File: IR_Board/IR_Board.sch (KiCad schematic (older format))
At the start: 16 parts, among them J1 Conn_02x08_Row_Letter_First, U1 TSSP58038, U10 TSSP58038, U11 TSSP58038, U12 TSSP58038, U13 TSSP58038, U14 TSSP58038, U2 TSSP58038, U3 TSSP58038, U4 TSSP58038, U5 TSSP58038, U6 TSSP58038, U7 TSSP58038, U8 TSSP58038, U9 TSSP58038

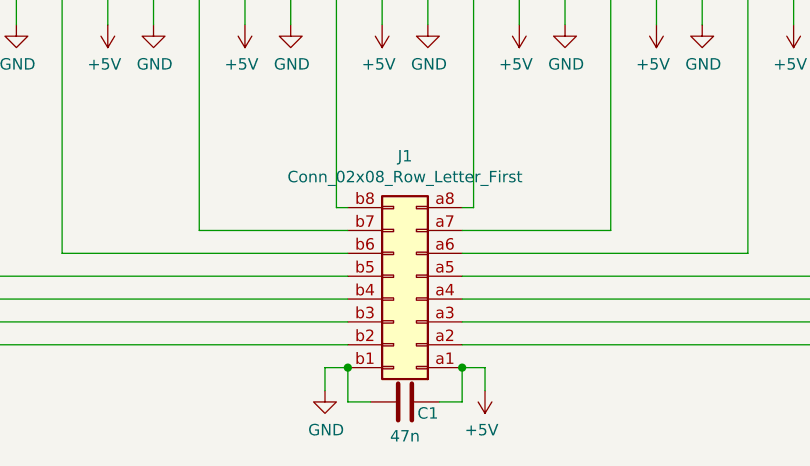
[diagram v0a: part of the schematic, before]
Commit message: motor drivers added
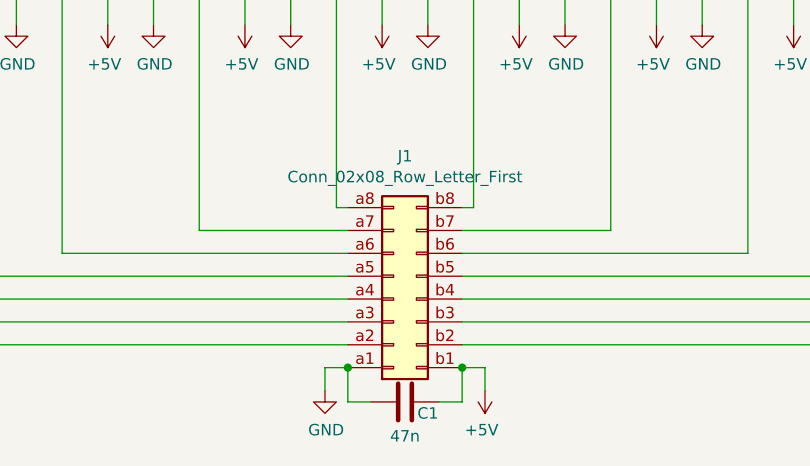
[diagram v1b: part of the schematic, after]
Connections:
- net +5V: now also J1.b1 (Pin_b1); no longer J1.a1 (Pin_a1)
- net GND: now also J1.a1 (Pin_a1); no longer J1.b1 (Pin_b1)
- net at U1.1 (OUT): now also J1.a2 (Pin_a2); no longer J1.b2 (Pin_b2)
- net at U2.1 (OUT): now also J1.a3 (Pin_a3); no longer J1.b3 (Pin_b3)
- net at U3.1 (OUT): now also J1.a4 (Pin_a4); no longer J1.b4 (Pin_b4)
- net at U4.1 (OUT): now also J1.a5 (Pin_a5); no longer J1.b5 (Pin_b5)
- net at U5.1 (OUT): now also J1.a6 (Pin_a6); no longer J1.b6 (Pin_b6)
- net at U6.1 (OUT): now also J1.a7 (Pin_a7); no longer J1.b7 (Pin_b7)
- net at U7.1 (OUT): now also J1.a8 (Pin_a8); no longer J1.b8 (Pin_b8)
- net at U8.1 (OUT): now also J1.b8 (Pin_b8); no longer J1.a8 (Pin_a8)
- net at U9.1 (OUT): now also J1.b7 (Pin_b7); no longer J1.a7 (Pin_a7)
- net at U10.1 (OUT): now also J1.b6 (Pin_b6); no longer J1.a6 (Pin_a6)
- net at U11.1 (OUT): now also J1.b5 (Pin_b5); no longer J1.a5 (Pin_a5)
- net at U12.1 (OUT): now also J1.b4 (Pin_b4); no longer J1.a4 (Pin_a4)
- net at U13.1 (OUT): now also J1.b3 (Pin_b3); no longer J1.a3 (Pin_a3)
- net at U14.1 (OUT): now also J1.b2 (Pin_b2); no longer J1.a2 (Pin_a2)
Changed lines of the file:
@@
 Wire Wire Line
 	9950 1900 9950 1750
-$Comp
-L Connector_Generic:Conn_02x08_Row_Letter_First J1
-U 1 1 61A6AA53
-P 5900 3100
-F 0 "J1" H 5950 2475 50  0000 C CNN
-F 1 "Conn_02x08_Row_Letter_First" H 5950 2566 50  0000 C CNN
-F 2 "Connector_JST:JST_PHD_B16B-PHDSS_2x08_P2.00mm_Vertical" H 5900 3100 50  0001 C CNN
-F 3 "~" H 5900 3100 50  0001 C CNN
-	1    5900 3100
-	-1   0    0    1
-$EndComp
 Wire Wire Line
 	1950 1750 1950 3300
@@
 	6150 2700 6150 1750
 Wire Wire Line
-	6100 2800 6750 2800
-Wire Wire Line
 	6750 2800 6750 1750
 Wire Wire Line
 	7350 1750 7350 2900
 Wire Wire Line
-	7350 2900 6100 2900
-Wire Wire Line
 	7950 1750 7950 3000
-Wire Wire Line
-	7950 3000 6100 3000
 Wire Wire Line
 	8550 1750 8550 3100
 Wire Wire Line
-	8550 3100 6100 3100
-Wire Wire Line
 	9150 1750 9150 3200
 Wire Wire Line
-	9150 3200 6100 3200
-Wire Wire Line
 	9750 1750 9750 3300
-Wire Wire Line
-	9750 3300 6100 3300
 $Comp
 L power:+5V #PWR0129
@@
 Wire Wire Line
 	5600 3550 5600 3400
-Connection ~ 5600 3400
 Wire Wire Line
 	6000 3550 6100 3550
@@
 	6100 3550 6100 3400
 Connection ~ 6100 3400
+Connection ~ 5600 3400
+Wire Wire Line
+	6100 2800 6750 2800
+Wire Wire Line
+	7350 2900 6100 2900
+Wire Wire Line
+	7950 3000 6100 3000
+Wire Wire Line
+	8550 3100 6100 3100
+Wire Wire Line
+	9150 3200 6100 3200
+Wire Wire Line
+	9750 3300 6100 3300
+$Comp
+L Connector_Generic:Conn_02x08_Row_Letter_First J1
+U 1 1 61A6AA53
+P 5800 3100
+F 0 "J1" H 5850 2475 50  0000 C CNN
+F 1 "Conn_02x08_Row_Letter_First" H 5850 2566 50  0000 C CNN
+F 2 "Connector_JST:JST_PHD_B16B-PHDSS_2x08_P2.00mm_Vertical" H 5800 3100 50  0001 C CNN
+F 3 "~" H 5800 3100 50  0001 C CNN
+	1    5800 3100
+	1    0    0    1
+$EndComp
 $EndSCHEMATC

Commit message: Started Light PCB
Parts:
- added C10, C11, C12, C13, C14, C15, C2, C3, C4, C5, C6, C7, C8, C9: 220n, Capacitor_SMD:C_0603_1608Metric_Pad1.08x0.95mm_HandSolder, symbol Device:C_Small
- added D1: B, LED_SMD:LED_0805_2012Metric_Pad1.15x1.40mm_HandSolder, symbol Device:LED
- added D2: A, LED_SMD:LED_0805_2012Metric_Pad1.15x1.40mm_HandSolder, symbol Device:LED_ALT
- added Q1, Q10, Q11, Q12, Q13, Q14, Q2, Q3, Q4, Q5, Q6, Q7, Q8, Q9: FDG1024NZ, Package_TO_SOT_SMD:SOT-363_SC-70-6, symbol Transistor_FET:FDG1024NZ
- added R1, R10, R11, R12, R13, R14, R15, R16, R17, R2, R3, R4, R5, R6, R7, R8, R9: 10k, Resistor_SMD:R_0603_1608Metric_Pad0.98x0.95mm_HandSolder, symbol Device:R_Small
- added SW1: SW_SPDT, Connector_PinHeader_2.54mm:PinHeader_1x03_P2.54mm_Vertical, symbol Switch:SW_SPDT
- C1: footprint Capacitor_SMD:C_0603_1608Metric_Pad1.05x0.95mm_HandSolder -> Capacitor_SMD:C_0603_1608Metric_Pad1.08x0.95mm_HandSolder
- J1: value Conn_02x08_Row_Letter_First -> CONN_OUT
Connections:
- net +5V: now also R9.2, SW1.2 (B)
- net GND: now also C10.1, C11.1, C12.1, C13.1, C14.1, C15.1, C2.1, C3.1, C4.1, C5.1, C6.1, C7.1, C8.1, C9.1, D1.1 (K), D2.1 (K), R9.1
- net at U1.1 (OUT): now also Q1.6 (D), Q2.6 (D); no longer J1.a2 (Pin_a2)
- net at U2.1 (OUT): now also Q3.6 (D), Q4.6 (D); no longer J1.a3 (Pin_a3)
- net at U3.1 (OUT): now also Q5.6 (D), Q6.6 (D); no longer J1.a4 (Pin_a4)
- net at U4.1 (OUT): now also Q7.6 (D), Q8.6 (D); no longer J1.a5 (Pin_a5)
- net at U5.1 (OUT): now also Q10.3 (D), Q9.3 (D); no longer J1.a6 (Pin_a6)
- net at U6.1 (OUT): now also Q11.6 (D), Q12.6 (D); no longer J1.a7 (Pin_a7)
- net at U7.1 (OUT): now also Q13.6 (D), Q14.6 (D); no longer J1.a8 (Pin_a8)
- net at U8.1 (OUT): now also Q1.3 (D), Q2.3 (D); no longer J1.b8 (Pin_b8)
- net at U9.1 (OUT): now also Q3.3 (D), Q4.3 (D); no longer J1.b7 (Pin_b7)
- net at U10.1 (OUT): now also Q5.3 (D), Q6.3 (D); no longer J1.b6 (Pin_b6)
- net at U11.1 (OUT): now also Q7.3 (D), Q8.3 (D); no longer J1.b5 (Pin_b5)
- net at U12.1 (OUT): now also Q10.6 (D), Q9.6 (D); no longer J1.b4 (Pin_b4)
- net at U13.1 (OUT): now also Q11.3 (D), Q12.3 (D); no longer J1.b3 (Pin_b3)
- net at U14.1 (OUT): now also Q13.3 (D), Q14.3 (D); no longer J1.b2 (Pin_b2)
- new net: C2.2, J1.a2 (Pin_a2), Q1.1 (S), R2.2
- new net: C4.2, J1.a3 (Pin_a3), Q3.1 (S), R4.2
- new net: C6.2, J1.a4 (Pin_a4), Q5.1 (S), R6.2
- new net: C8.2, J1.a5 (Pin_a5), Q7.1 (S), R8.2
- new net: J1.a6 (Pin_a6), Q9.4 (S)
- new net: J1.a7 (Pin_a7), Q11.1 (S), R15.2
- new net: J1.a8 (Pin_a8), Q13.1 (S), R17.2
- new net: C3.2, J1.b2 (Pin_b2), Q2.4 (S), R1.2
- new net: C5.2, J1.b3 (Pin_b3), Q4.4 (S), R3.2
- new net: C7.2, J1.b4 (Pin_b4), Q6.4 (S), R5.2
- new net: C9.2, J1.b5 (Pin_b5), Q8.4 (S), R7.2
- new net: C10.2, J1.b6 (Pin_b6), Q10.1 (S), R10.2
- new net: C13.2, J1.b7 (Pin_b7), Q12.4 (S), R14.2
- new net: C15.2, J1.b8 (Pin_b8), Q14.4 (S), R16.2
- new net: Q2.1 (S), R2.1
- new net: Q4.1 (S), R4.1
- new net: Q6.1 (S), R6.1
- new net: Q8.1 (S), R8.1
- new net: Q10.4 (S), R11.1
- new net: Q12.1 (S), R15.1
- new net: Q14.1 (S), R17.1
- new net: Q13.4 (S), R16.1
- new net: Q11.4 (S), R14.1
- new net: Q9.1 (S), R10.1
- new net: Q7.4 (S), R7.1
- new net: Q5.4 (S), R5.1
- new net: Q3.4 (S), R3.1
- new net: Q1.4 (S), R1.1
- new net: C11.2, R11.2
- new net: D2.2 (A), R13.1
- new net: D1.2 (A), R12.1
- new net A: Q1.2 (G), Q1.5 (G), Q10.2 (G), Q11.2 (G), Q12.5 (G), Q13.2 (G), Q14.5 (G), Q2.5 (G), Q3.2 (G), Q4.5 (G), Q5.2 (G), Q6.5 (G), Q7.2 (G), Q8.5 (G), Q9.5 (G), R13.2, SW1.3 (C)
- new net B: Q10.5 (G), Q11.5 (G), Q12.2 (G), Q13.5 (G), Q14.2 (G), Q2.2 (G), Q3.5 (G), Q4.2 (G), Q5.5 (G), Q6.2 (G), Q7.5 (G), Q8.2 (G), Q9.2 (G), R12.2, SW1.1 (A)
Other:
- moved on the sheet: C1, J1, U1, U10, U11, U12, U13, U14, U2, U3, U4, U5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

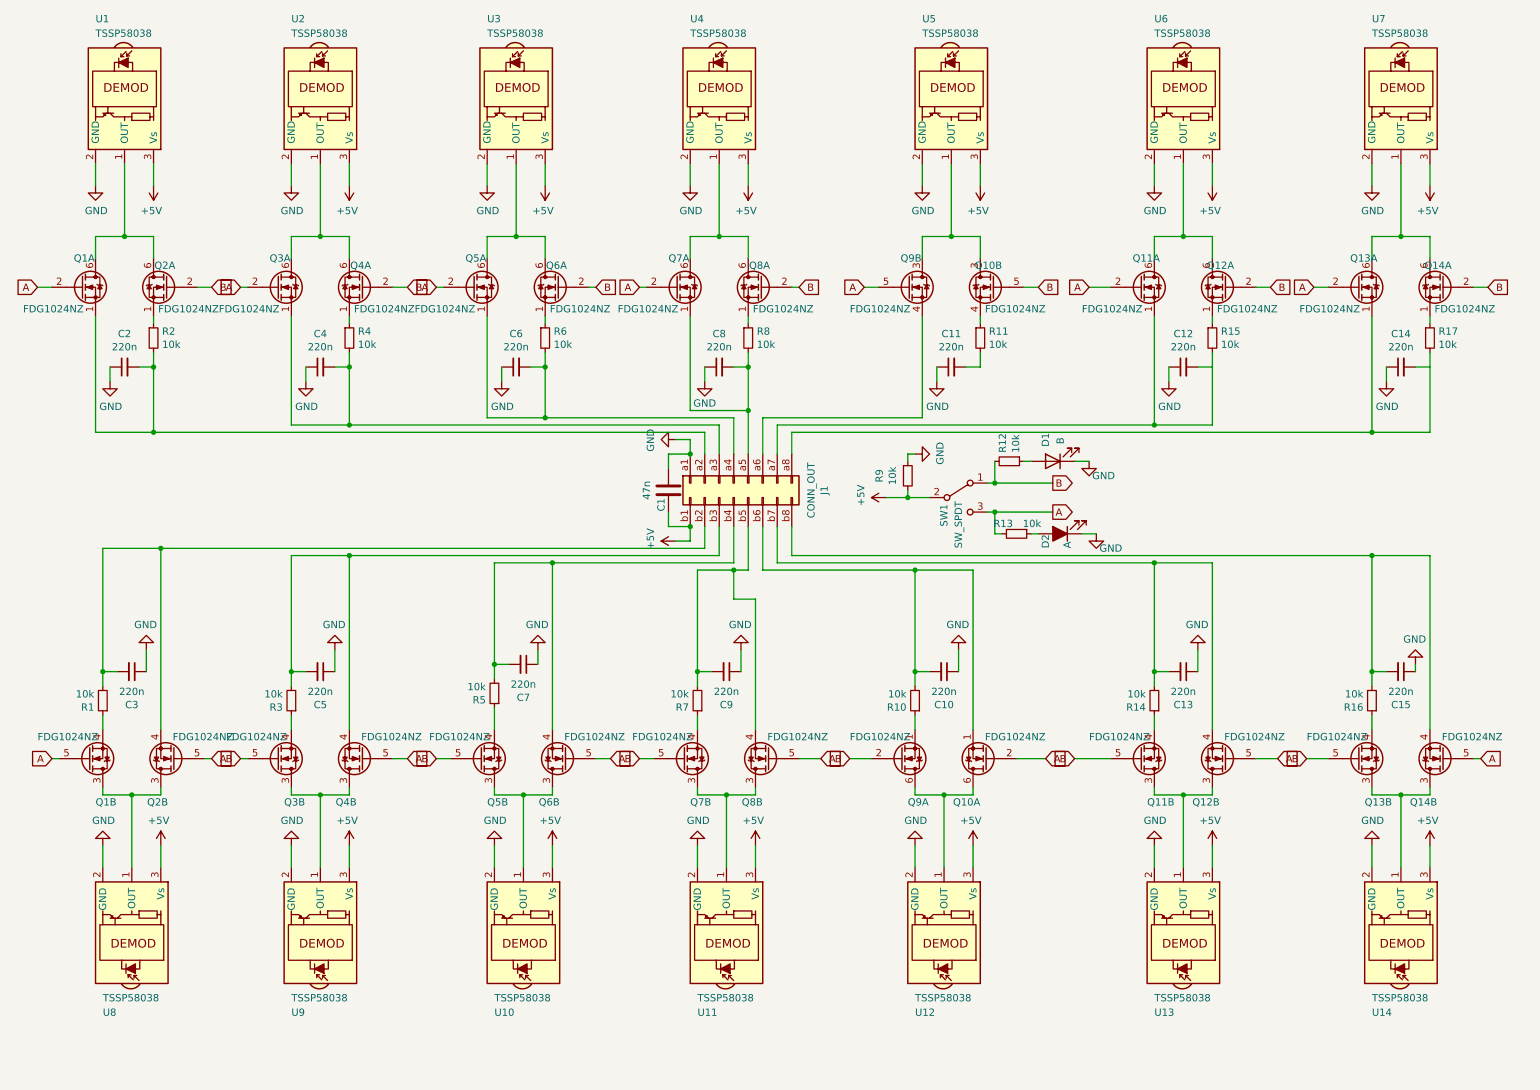
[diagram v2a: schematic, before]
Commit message: Finalized Pin layout, started redesigned Buck
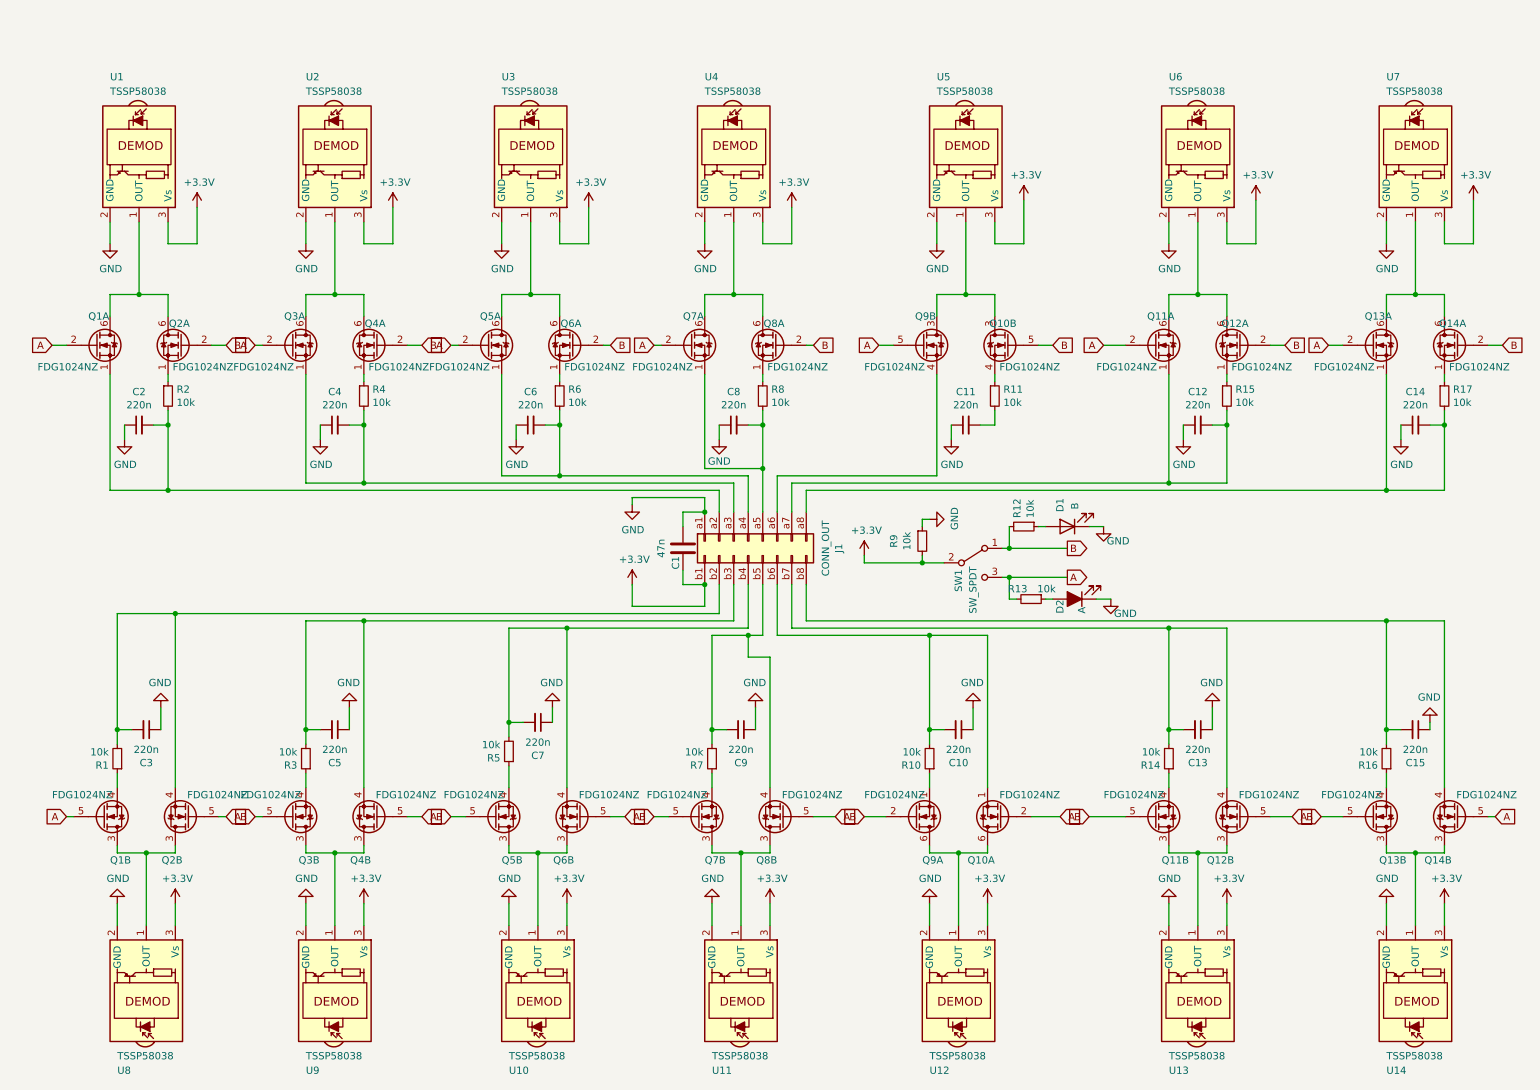
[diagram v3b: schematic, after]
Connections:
- net at J1.a7 (Pin_a7), Q11.1 (S), R15.2: now also C12.2
- net at J1.a8 (Pin_a8), Q13.1 (S), R17.2: now also C14.2
- net +5V renamed +3V3
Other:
- moved on the sheet: C1, C10, C11, C12, C13, C14, C15, C2, C3, C4, C5, C6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

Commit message: Started IR PCB
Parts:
- removed J1: CONN_OUT, Connector_JST:JST_PHD_B16B-PHDSS_2x08_P2.00mm_Vertical, symbol Connector_Generic:Conn_02x08_Row_Letter_First
- removed Q1, Q10, Q11, Q12, Q13, Q14, Q2, Q3, Q4, Q5, Q6, Q7, Q8, Q9: FDG1024NZ, Package_TO_SOT_SMD:SOT-363_SC-70-6, symbol Transistor_FET:FDG1024NZ
- added J1: Conn_02x08_Top_Bottom, Connector_Hirose:Hirose_DF11-16DP-2DSA_2x08_P2.00mm_Vertical, symbol Connector_Generic:Conn_02x08_Top_Bottom
- added Q1, Q10, Q11, Q12, Q13, Q14, Q2, Q3, Q4, Q5, Q6, Q7, Q8, Q9: FDG6335N, Package_TO_SOT_SMD:SOT-363_SC-70-6, symbol Transistor_FET:FDG6335N
- C1, C10, C11, C12, C13, C14, C15, C2, C3, C4, C5, C6, C7, C8, C9: footprint Capacitor_SMD:C_0603_1608Metric_Pad1.08x0.95mm_HandSolder -> Capacitor_SMD:C_0603_1608Metric
- R1, R10, R11, R12, R13, R14, R15, R16, R17, R2, R3, R4, R5, R6, R7, R8, R9: footprint Resistor_SMD:R_0603_1608Metric_Pad0.98x0.95mm_HandSolder -> Resistor_SMD:R_0603_1608Metric
- SW1: footprint Connector_PinHeader_2.54mm:PinHeader_1x03_P2.54mm_Vertical -> Main_Board:EG1218
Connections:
- net +3V3: now also J1.9 (Pin_9)
- net A: now also Q1.2 (G), Q10.2 (G), Q11.2 (G), Q12.2 (G), Q13.2 (G), Q14.2 (G), Q2.2 (G), Q3.2 (G), Q4.2 (G), Q5.2 (G), Q6.2 (G), Q7.2 (G), Q8.2 (G), Q9.2 (G)
- net B: now also Q1.5 (G), Q10.5 (G), Q11.5 (G), Q12.5 (G), Q13.5 (G), Q14.5 (G), Q2.5 (G), Q3.5 (G), Q4.5 (G), Q5.5 (G), Q6.5 (G), Q7.5 (G), Q8.5 (G), Q9.5 (G)
- net GND: now also J1.1 (Pin_1)
- net at U1.1 (OUT): now also Q1.3 (D), Q1.6 (D)
- net at U2.1 (OUT): now also Q2.3 (D), Q2.6 (D)
- net at U3.1 (OUT): now also Q3.3 (D), Q3.6 (D)
- net at U4.1 (OUT): now also Q4.3 (D), Q4.6 (D)
- net at U5.1 (OUT): now also Q5.3 (D), Q5.6 (D)
- net at U6.1 (OUT): now also Q6.3 (D), Q6.6 (D)
- net at U7.1 (OUT): now also Q7.3 (D), Q7.6 (D)
- net at U8.1 (OUT): now also Q8.3 (D), Q8.6 (D)
- net at U9.1 (OUT): now also Q9.3 (D), Q9.6 (D)
- net at U10.1 (OUT): now also Q10.3 (D), Q10.6 (D)
- net at U11.1 (OUT): now also Q11.3 (D), Q11.6 (D)
- net at U12.1 (OUT): now also Q12.3 (D), Q12.6 (D)
- net at U13.1 (OUT): now also Q13.3 (D), Q13.6 (D)
- net at U14.1 (OUT): now also Q14.3 (D), Q14.6 (D)
- net at C2.2, R2.2: now also J1.2 (Pin_2), Q1.1 (S)
- net at C4.2, R4.2: now also J1.3 (Pin_3), Q2.1 (S)
- net at C6.2, R6.2: now also J1.4 (Pin_4), Q3.1 (S)
- net at C8.2, R8.2: now also J1.5 (Pin_5), Q4.1 (S)
- net at C12.2, R15.2: now also J1.7 (Pin_7), Q6.1 (S)
- net at C14.2, R17.2: now also J1.8 (Pin_8), Q7.1 (S)
- net at C3.2, R1.2: now also J1.10 (Pin_10), Q8.1 (S)
- net at C5.2, R3.2: now also J1.11 (Pin_11), Q9.1 (S)
- net at C7.2, R5.2: now also J1.12 (Pin_12), Q10.1 (S)
- net at C9.2, R7.2: now also J1.13 (Pin_13), Q11.1 (S)
- net at C10.2, R10.2: now also J1.14 (Pin_14), Q12.1 (S)
- net at C13.2, R14.2: now also J1.15 (Pin_15), Q13.1 (S)
- net at C15.2, R16.2: now also J1.16 (Pin_16), Q14.1 (S)
- net at R2.1: now also Q1.4 (S)
- net at R4.1: now also Q2.4 (S)
- net at R6.1: now also Q3.4 (S)
- net at R8.1: now also Q4.4 (S)
- net at R11.1: now also Q5.4 (S)
- net at R15.1: now also Q6.4 (S)
- net at R17.1: now also Q7.4 (S)
- net at R16.1: now also Q14.4 (S)
- net at R14.1: now also Q13.4 (S)
- net at R10.1: now also Q12.4 (S)
- net at R7.1: now also Q11.4 (S)
- net at R5.1: now also Q10.4 (S)
- net at R3.1: now also Q9.4 (S)
- net at R1.1: now also Q8.4 (S)
- net at C11.2, R11.2: now also J1.6 (Pin_6), Q5.1 (S)
